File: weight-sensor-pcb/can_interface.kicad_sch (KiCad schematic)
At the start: 0 parts

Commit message: Add Serial Connection and CAN Transceiver
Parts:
- added IC1: SN65HVD230DR, SOT127P600X175-8N, symbol Capstone:SN65HVD230DR
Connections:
- new net +3.3V: IC1.3 (VCC)
- new net CANH: IC1.7 (CANH)
- new net CANL: IC1.6 (CANL)
- new net CAN_RX: IC1.4 (R)
- new net CAN_TX: IC1.1 (D)
- new net GND: IC1.2 (GND)

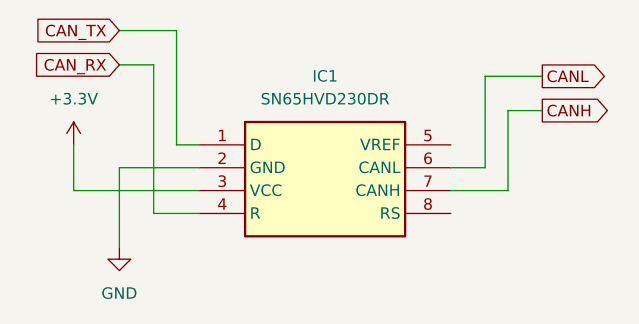
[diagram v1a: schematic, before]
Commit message: Add hierarchial labels to MCU and CAN Interface sheets
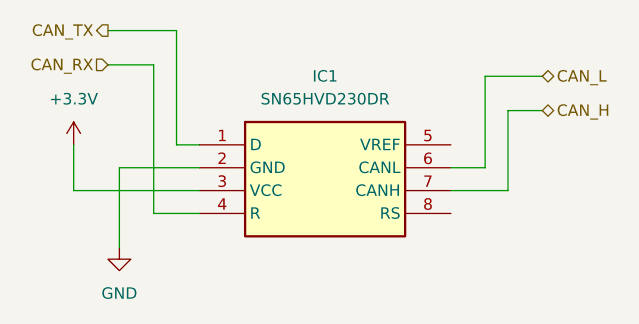
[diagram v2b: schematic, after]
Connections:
- net CANH renamed CAN_H
- net CANL renamed CAN_L
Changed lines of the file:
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@@
+	(wire
+		(pts
+			(xy 120.65 77.47) (xy 125.73 77.47)
+		)
+		(stroke
+			(width 0)
+			(type default)
+		)
+	)
 	(wire
 		(pts
@@
 	(wire
 		(pts
-			(xy 121.92 73.66) (xy 128.27 73.66)
-		)
-		(stroke
-			(width 0)
-			(type default)
-		)
-	)
-	(wire
-		(pts
-			(xy 121.92 77.47) (xy 125.73 77.47)
+			(xy 120.65 73.66) (xy 128.27 73.66)
 		)
 		(stroke
@@
 		)
 	)
-	(global_label "CAN_TX"
+	(hierarchical_label "CAN_RX"
 		(shape input)
-		(at 121.92 73.66 180)
-		(fields_autoplaced yes)
+		(at 120.65 77.47 180)
 		(effects
 			(font
@@
 			(justify right)
 		)
-		(property "Intersheetrefs" "${INTERSHEET_REFS}"
-			(at 112.101 73.66 0)
-			(effects
-				(font
-					(size 1.27 1.27)
-				)
-				(justify right)
-				(hide yes)
+	)
+	(hierarchical_label "CAN_TX"
+		(shape output)
+		(at 120.65 73.66 180)
+		(effects
+			(font
+				(size 1.27 1.27)
 			)
+			(justify right)
 		)
 	)
-	(global_label "CANL"
-		(shape output)
+	(hierarchical_label "CAN_L"
+		(shape bidirectional)
 		(at 168.91 78.74 0)
-		(fields_autoplaced yes)
 		(effects
 			(font
@@
 			(justify left)
 		)
-		(property "Intersheetrefs" "${INTERSHEET_REFS}"
-			(at 176.6124 78.74 0)
-			(effects
-				(font
-					(size 1.27 1.27)
-				)
-				(justify left)
-				(hide yes)
-			)
-		)
 	)
-	(global_label "CANH"
-		(shape output)
+	(hierarchical_label "CAN_H"
+		(shape bidirectional)
 		(at 168.91 82.55 0)
-		(fields_autoplaced yes)
 		(effects
 			(font
@@
 			(justify left)
 		)
-		(property "Intersheetrefs" "${INTERSHEET_REFS}"
-			(at 176.9148 82.55 0)
-			(effects
-				(font
-					(size 1.27 1.27)
-				)
-				(justify left)
-				(hide yes)
-			)
-		)
 	)
-	(global_label "CAN_RX"
-		(shape input)
-		(at 121.92 77.47 180)
-		(fields_autoplaced yes)
-		(effects
-			(font
-				(size 1.27 1.27)
-			)
-			(justify right)
-		)
-		(property "Intersheetrefs" "${INTERSHEET_REFS}"
-			(at 111.7986 77.47 0)
-			(effects
-				(font
-					(size 1.27 1.27)
-				)
-				(justify right)
-				(hide yes)
-			)
-		)
-	)

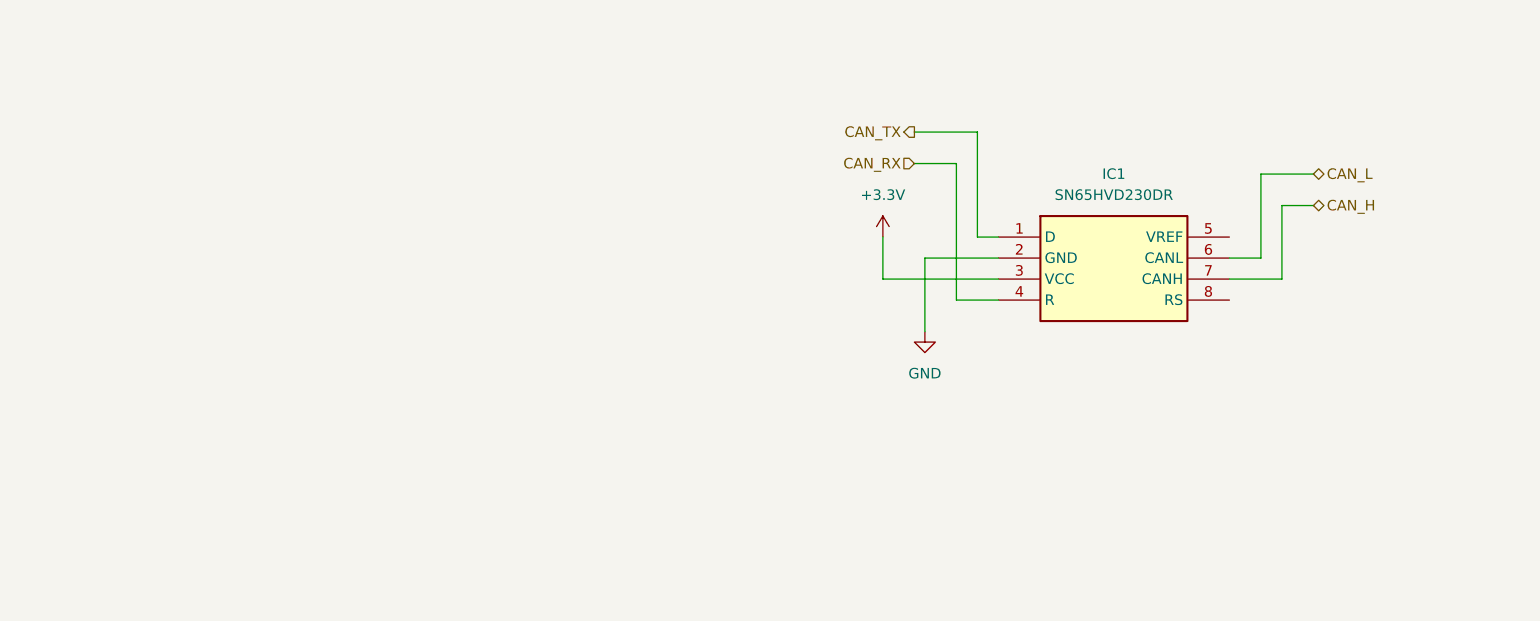
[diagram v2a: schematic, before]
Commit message: Add decoupling capacitors, current limiting resistors for MCU and CAN Transceiver
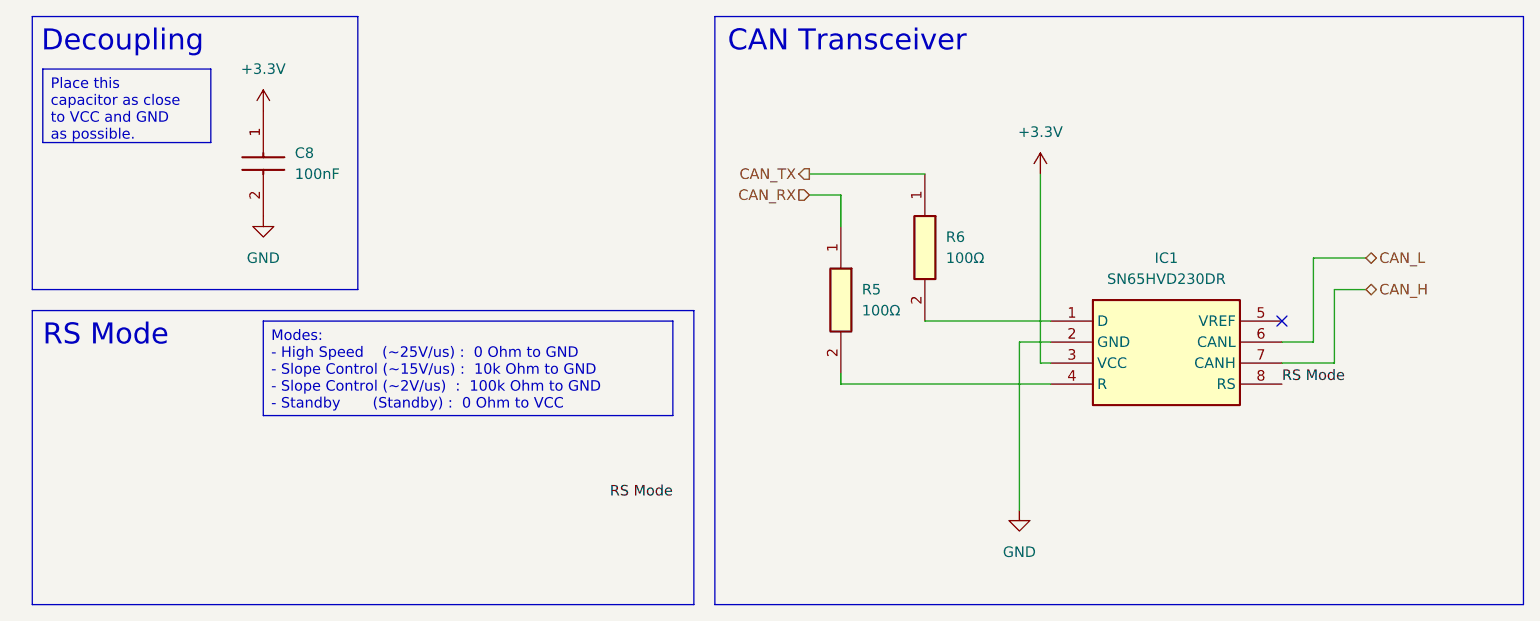
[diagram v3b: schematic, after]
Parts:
- added C8: 100nF, CAPC1005X70N, symbol Capstone:GRM155R70J104KA01D
- added R5, R6: 100Ω, RESC1608X55N, symbol Capstone:RC0603FR-07100RL
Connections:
- net +3.3V: now also C8.1
- net CAN_RX: now also R5.1; no longer IC1.4 (R)
- net CAN_TX: now also R6.1; no longer IC1.1 (D)
- net GND: now also C8.2
- net RS Mode: now reaches IC1.8 (RS)
- new net: IC1.1 (D), R6.2
- new net: IC1.4 (R), R5.2
- no-connect marks 0 -> 1
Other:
- note added: "CAN Transceiver"
- note added: "Decoupling"
- note added: "RS Mode"
- moved on the sheet: IC1

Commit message: Add Test points, CAN connector, USART connector
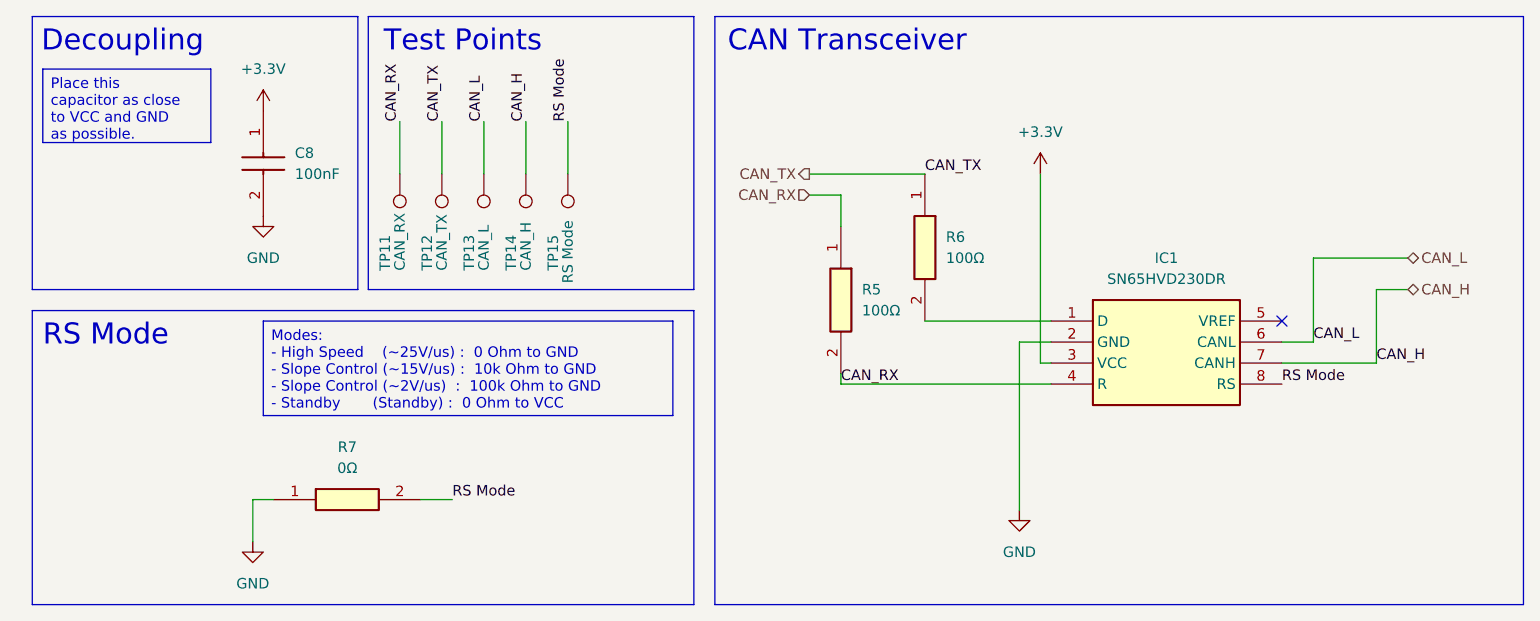
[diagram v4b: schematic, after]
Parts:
- added R7: 0Ω, RESC1608X55N, symbol Capstone:RC0603JR-070RL
- added TP11: CAN_RX, symbol Connector:TestPoint
- added TP12: CAN_TX, symbol Connector:TestPoint
- added TP13: CAN_L, symbol Connector:TestPoint
- added TP14: CAN_H, symbol Connector:TestPoint
- added TP15: RS Mode, symbol Connector:TestPoint
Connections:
- net CAN_H: now also TP14.1
- net CAN_L: now also TP13.1
- net CAN_RX: now also IC1.4 (R), R5.2, TP11.1
- net CAN_TX: now also TP12.1
- net GND: now also R7.1
- net RS Mode: now also R7.2, TP15.1
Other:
- note added: "Test Points"

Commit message: initial PCB layout design
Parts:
- TP11, TP12, TP13, TP14, TP15: footprint (none) -> TestPoint:TestPoint_Pad_D1.5mm
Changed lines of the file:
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@@
 			)
 		)
-		(property "Footprint" ""
+		(property "Footprint" "TestPoint:TestPoint_Pad_D1.5mm"
 			(at 63.5 78.74 0)
 			(effects
@@
 			)
 		)
-		(property "Footprint" ""
+		(property "Footprint" "TestPoint:TestPoint_Pad_D1.5mm"
 			(at 73.66 78.74 0)
 			(effects
@@
 			)
 		)
-		(property "Footprint" ""
+		(property "Footprint" "TestPoint:TestPoint_Pad_D1.5mm"
 			(at 53.34 78.74 0)
 			(effects
@@
 			)
 		)
-		(property "Footprint" ""
+		(property "Footprint" "TestPoint:TestPoint_Pad_D1.5mm"
 			(at 58.42 78.74 0)
 			(effects
@@
 			)
 		)
-		(property "Footprint" ""
+		(property "Footprint" "TestPoint:TestPoint_Pad_D1.5mm"
 			(at 68.58 78.74 0)
 			(effects

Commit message: Layout draft complete
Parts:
- renumbered C8 to C17, IC1 to IC7, R7 to R23, R5 to R24, R6 to R25, TP11 to TP17, TP12 to TP18, TP13 to TP19, TP14 to TP20, TP15 to TP21
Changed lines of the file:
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@@
 		(dnp no)
 		(fields_autoplaced yes)
-		(property "Reference" "C8"
+		(property "Reference" "C17"
 			(at 45.72 76.1999 90)
 			(effects
@@
 			(project ""
 				(path "/030ca1f5-68f0-4323-9a91-656d7965b13e/29936029-5fc3-43fa-9698-e8fdd966363b"
-					(reference "C8")
+					(reference "C17")
 					(unit 1)
 				)
@@
 		(dnp no)
 		(fields_autoplaced yes)
-		(property "Reference" "R7"
+		(property "Reference" "R23"
 			(at 52.07 111.76 0)
 			(effects
@@
 			(project ""
 				(path "/030ca1f5-68f0-4323-9a91-656d7965b13e/29936029-5fc3-43fa-9698-e8fdd966363b"
-					(reference "R7")
+					(reference "R23")
 					(unit 1)
 				)
@@
 		(on_board yes)
 		(dnp no)
-		(property "Reference" "TP13"
+		(property "Reference" "TP19"
 			(at 66.802 90.424 90)
 			(effects
@@
 			(project "weight-sensor-pcb"
 				(path "/030ca1f5-68f0-4323-9a91-656d7965b13e/29936029-5fc3-43fa-9698-e8fdd966363b"
-					(reference "TP13")
+					(reference "TP19")
 					(unit 1)
 				)
@@
 		(dnp no)
 		(fields_autoplaced yes)
-		(property "Reference" "#PWR028"
+		(property "Reference" "#PWR034"
 			(at 40.64 129.54 0)
 			(effects
@@
 			(project ""
 				(path "/030ca1f5-68f0-4323-9a91-656d7965b13e/29936029-5fc3-43fa-9698-e8fdd966363b"
-					(reference "#PWR028")
+					(reference "#PWR034")
 					(unit 1)
 				)
@@
 		(on_board yes)
 		(dnp no)
-		(property "Reference" "TP15"
+		(property "Reference" "TP21"
 			(at 76.962 90.424 90)
 			(effects
@@
 			(project "weight-sensor-pcb"
 				(path "/030ca1f5-68f0-4323-9a91-656d7965b13e/29936029-5fc3-43fa-9698-e8fdd966363b"
-					(reference "TP15")
+					(reference "TP21")
 					(unit 1)
 				)
@@
 		(dnp no)
 		(fields_autoplaced yes)
-		(property "Reference" "#PWR015"
+		(property "Reference" "#PWR037"
 			(at 133.35 125.73 0)
 			(effects
@@
 			(project ""
 				(path "/030ca1f5-68f0-4323-9a91-656d7965b13e/29936029-5fc3-43fa-9698-e8fdd966363b"
-					(reference "#PWR015")
+					(reference "#PWR037")
 					(unit 1)
 				)
@@
 		(dnp no)
 		(fields_autoplaced yes)
-		(property "Reference" "#PWR016"
+		(property "Reference" "#PWR038"
 			(at 135.89 82.55 0)
 			(effects
@@
 			(project ""
 				(path "/030ca1f5-68f0-4323-9a91-656d7965b13e/29936029-5fc3-43fa-9698-e8fdd966363b"
-					(reference "#PWR016")
+					(reference "#PWR038")
 					(unit 1)
 				)
@@
 		(on_board yes)
 		(dnp no)
-		(property "Reference" "TP11"
+		(property "Reference" "TP17"
 			(at 56.642 90.424 90)
 			(effects
@@
 			(project ""
 				(path "/030ca1f5-68f0-4323-9a91-656d7965b13e/29936029-5fc3-43fa-9698-e8fdd966363b"
-					(reference "TP11")
+					(reference "TP17")
 					(unit 1)
 				)
@@
 		(dnp no)
 		(fields_autoplaced yes)
-		(property "Reference" "R6"
+		(property "Reference" "R25"
 			(at 124.46 86.3599 90)
 			(effects
@@
 			(project "weight-sensor-pcb"
 				(path "/030ca1f5-68f0-4323-9a91-656d7965b13e/29936029-5fc3-43fa-9698-e8fdd966363b"
-					(reference "R6")
+					(reference "R25")
 					(unit 1)
 				)
@@
 		(on_board yes)
 		(dnp no)
-		(property "Reference" "TP12"
+		(property "Reference" "TP18"
 			(at 61.722 90.424 90)
 			(effects
@@
 			(project "weight-sensor-pcb"
 				(path "/030ca1f5-68f0-4323-9a91-656d7965b13e/29936029-5fc3-43fa-9698-e8fdd966363b"
-					(reference "TP12")
+					(reference "TP18")
 					(unit 1)
 				)
@@
 		(dnp no)
 		(fields_autoplaced yes)
-		(property "Reference" "#PWR024"
+		(property "Reference" "#PWR035"
 			(at 41.91 74.93 0)
 			(effects
@@
 			(project ""
 				(path "/030ca1f5-68f0-4323-9a91-656d7965b13e/29936029-5fc3-43fa-9698-e8fdd966363b"
-					(reference "#PWR024")
+					(reference "#PWR035")
 					(unit 1)
 				)
@@
 		(on_board yes)
 		(dnp no)
-		(property "Reference" "TP14"
+		(property "Reference" "TP20"
 			(at 71.882 90.424 90)
 			(effects
@@
 			(project "weight-sensor-pcb"
 				(path "/030ca1f5-68f0-4323-9a91-656d7965b13e/29936029-5fc3-43fa-9698-e8fdd966363b"
-					(reference "TP14")
+					(reference "TP20")
 					(unit 1)
 				)
@@
 		(dnp no)
 		(fields_autoplaced yes)
-		(property "Reference" "#PWR025"
+		(property "Reference" "#PWR036"
 			(at 41.91 90.17 0)
 			(effects
@@
 			(project ""
 				(path "/030ca1f5-68f0-4323-9a91-656d7965b13e/29936029-5fc3-43fa-9698-e8fdd966363b"
-					(reference "#PWR025")
+					(reference "#PWR036")
 					(unit 1)
 				)
@@
 		(on_board yes)
 		(dnp no)
-		(property "Reference" "IC1"
+		(property "Reference" "IC7"
 			(at 151.13 88.9 0)
 			(effects
@@
 			(project ""
 				(path "/030ca1f5-68f0-4323-9a91-656d7965b13e/29936029-5fc3-43fa-9698-e8fdd966363b"
-					(reference "IC1")
+					(reference "IC7")
 					(unit 1)
 				)
@@
 		(dnp no)
 		(fields_autoplaced yes)
-		(property "Reference" "R5"
+		(property "Reference" "R24"
 			(at 114.3 92.7099 90)
 			(effects
@@
 			(project ""
 				(path "/030ca1f5-68f0-4323-9a91-656d7965b13e/29936029-5fc3-43fa-9698-e8fdd966363b"
-					(reference "R5")
-					(unit 1)
-				)
+					(reference "R24")
+					(unit 1)
+				)
